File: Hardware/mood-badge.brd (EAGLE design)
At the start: 100 x 80 mm, 0 parts

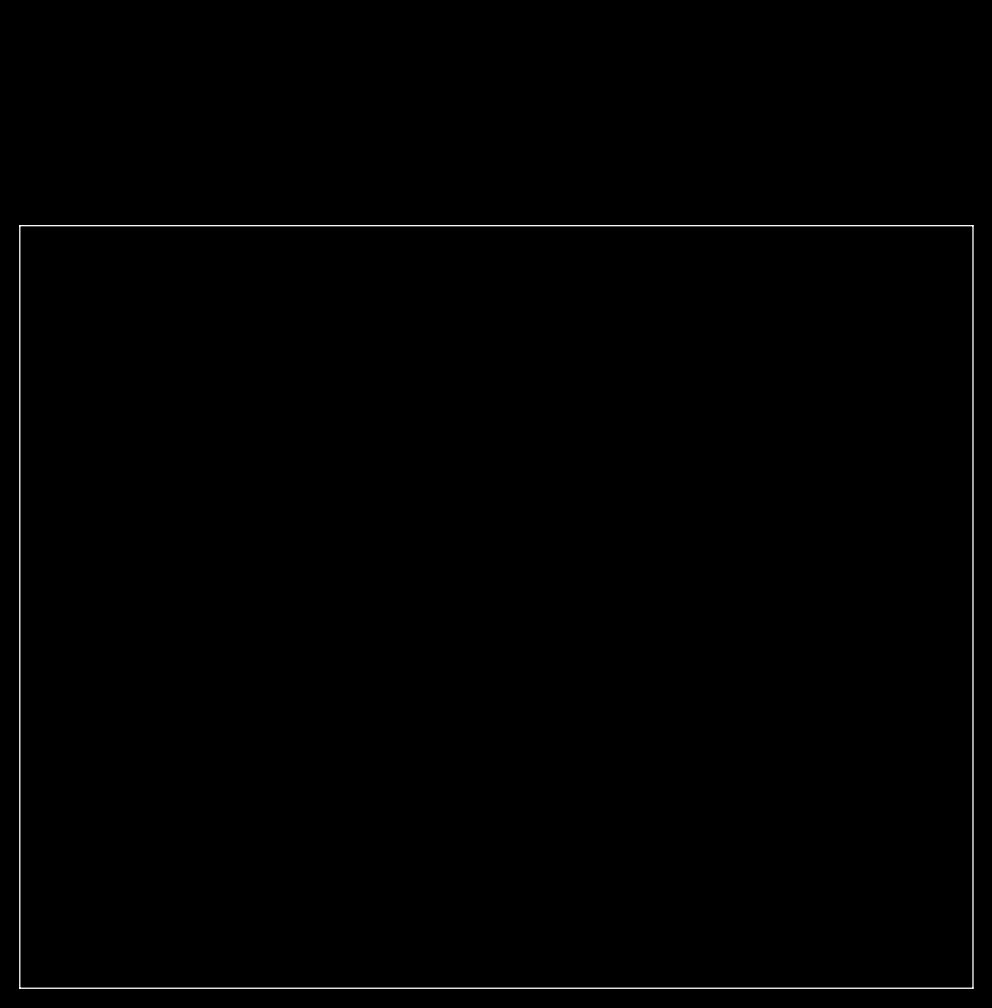
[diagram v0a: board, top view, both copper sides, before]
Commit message: PCB perimeter imported from Fusion 360 sketch
Will include Fusion 360 file later
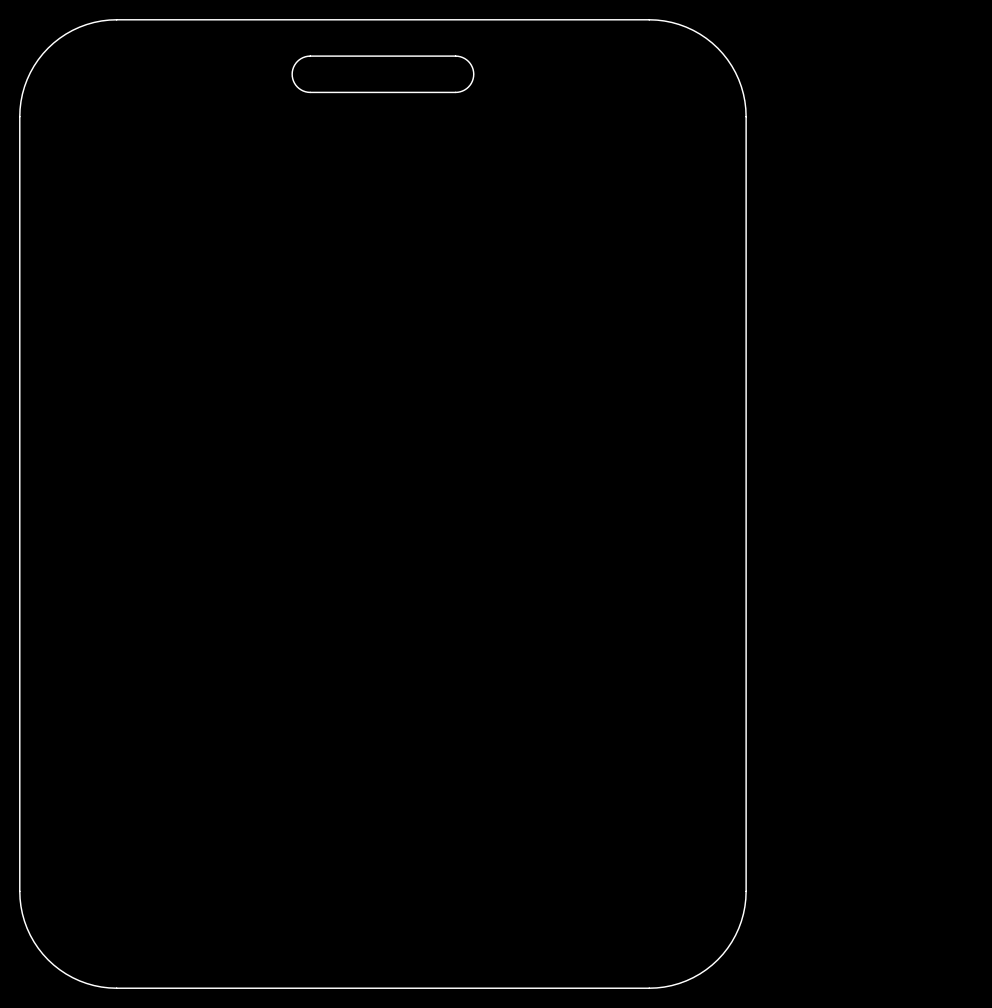
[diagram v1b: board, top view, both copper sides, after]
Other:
- board size 100 x 80 mm -> 76.2 x 101.6 mm
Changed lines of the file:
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@@
 <setting verticaltext="up"/>
 </settings>
-<grid distance="50" unitdist="mil" unit="mil" style="lines" multiple="1" display="no" altdistance="5" altunitdist="mil" altunit="mil"/>
+<grid distance="50" unitdist="mil" unit="mil" style="dots" multiple="1" display="yes" altdistance="5" altunitdist="mil" altunit="mil"/>
 <layers>
 <layer number="1" name="Top" color="4" fill="1" visible="yes" active="yes"/>
@@
 <layer number="43" name="vRestrict" color="2" fill="10" visible="yes" active="yes"/>
 <layer number="44" name="Drills" color="7" fill="1" visible="no" active="yes"/>
-<layer number="45" name="Holes" color="7" fill="1" visible="no" active="yes"/>
-<layer number="46" name="Milling" color="3" fill="1" visible="no" active="yes"/>
+<layer number="45" name="Holes" color="7" fill="1" visible="yes" active="yes"/>
+<layer number="46" name="Milling" color="3" fill="1" visible="yes" active="yes"/>
 <layer number="47" name="Measures" color="7" fill="1" visible="no" active="yes"/>
 <layer number="48" name="Document" color="7" fill="1" visible="yes" active="yes"/>
@@
 </layers>
 <board>
+<fusionsync huburn="a.YnVzaW5lc3M6cHVyZHVlMjM0NQ" projecturn="a.YnVzaW5lc3M6cHVyZHVlMjM0NSNEMjAyMTAyMjczODc2MTU2NzY" f3durn="urn:adsk.wipprod:dm.lineage:ZhKUu0ZCSQ-Y4oJNQzIvWw" pcbguid="" lastpulledtime="2021-02-27T19:33:12Z" lastsyncedchangeguid="" latestrevisionid="70cdc62d-c257-407d-8d81-74bbf69e218d" lastsyncedrevisionid="70cdc62d-c257-407d-8d81-74bbf69e218d" lastboardhashguid="" lastpushedtime="" linktopcb3d="true"/>
 <plain>
-<wire x1="0" y1="0" x2="100" y2="0" width="0" layer="20"/>
-<wire x1="100" y1="0" x2="100" y2="80" width="0" layer="20"/>
-<wire x1="100" y1="80" x2="0" y2="80" width="0" layer="20"/>
-<wire x1="0" y1="80" x2="0" y2="0" width="0" layer="20"/>
+<wire x1="30.48" y1="97.79" x2="30.48" y2="93.98" width="0.1524" layer="20" curve="180" locked="yes"/>
+<wire x1="30.48" y1="97.79" x2="45.72" y2="97.79" width="0.1524" layer="20" locked="yes"/>
+<wire x1="45.72" y1="93.98" x2="45.72" y2="97.79" width="0.1524" layer="20" curve="180" locked="yes"/>
+<wire x1="45.72" y1="93.98" x2="30.48" y2="93.98" width="0.1524" layer="20" locked="yes"/>
+<wire x1="0" y1="10.16" x2="10.16" y2="0" width="0.1524" layer="20" curve="90" locked="yes"/>
+<wire x1="10.16" y1="0" x2="66.04" y2="0" width="0.1524" layer="20" locked="yes"/>
+<wire x1="66.04" y1="0" x2="76.2" y2="10.16" width="0.1524" layer="20" curve="90" locked="yes"/>
+<wire x1="76.2" y1="10.16" x2="76.2" y2="91.44" width="0.1524" layer="20" locked="yes"/>
+<wire x1="76.2" y1="91.44" x2="66.04" y2="101.6" width="0.1524" layer="20" curve="90" locked="yes"/>
+<wire x1="66.04" y1="101.6" x2="10.16" y2="101.6" width="0.1524" layer="20" locked="yes"/>
+<wire x1="10.16" y1="101.6" x2="0" y2="91.44" width="0.1524" layer="20" curve="90" locked="yes"/>
+<wire x1="0" y1="91.44" x2="0" y2="10.16" width="0.1524" layer="20" locked="yes"/>
 </plain>
 <attributes>
@@
 </board>
 </drawing>
+<compatibility>
+<note version="8.3" severity="warning">
+Since Version 8.3, EAGLE supports Fusion synchronisation.
+This feature will not be available in this version and saving
+the document will break the link to the Fusion PCB feature.
+</note>
+<note version="8.5" severity="warning">
+Since Version 8.5, EAGLE supports locking for holes, vias, wires and polygons.
+The locking property on all objects of these types will not be understood in this version.
+</note>
+</compatibility>
 </eagle>
